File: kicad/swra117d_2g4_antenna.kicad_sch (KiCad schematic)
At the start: 5 parts, among them J1 SMA edge launch

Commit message: Fix the ERC error and the lib_symbol_mismatch warnings
A KiCad 9 ERC run reported 1 error and 8 warnings, all from where the
schematic's symbols come from rather than from its wiring.

power_pin_not_driven on #PWR01: the board is entirely passive, so nothing
drives the ground net as far as ERC is concerned. Added #FLG01, a PWR_FLAG
with a power-output pin, on that net.

lib_symbol_mismatch on C1, C2, L1, J1 and the four ground symbols: a
schematic embeds a copy of every symbol it places, and the embedded
stand-ins for Device:C, Device:L, Connector:Conn_Coaxial and power:GND did
not match the installed stock libraries. Moved all of them into
library/SWRA117D_RF.kicad_sym with the same pin geometry, so the schematic
embeds from an in-repo library and the two copies are identical by
construction - the same reason the antenna symbol never produced the
warning. The project no longer depends on the stock libraries at all.

check_project.py now enforces exactly that condition: every embedded symbol
must resolve to the project library and compare equal to it, and any
external lib_id is an error. Both cases are covered by mutation tests.

Nothing in the ERC report touched connectivity - the netlist was as
designed. DRC has not been run yet.

Co-Authored-By: Claude Opus 5 <noreply@anthropic.com>
Claude-Session: https://claude.ai/code/session_01Prj6bUQ2KQzzxzD4bgtswJ
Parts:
- C1, C2: symbol Device:C -> SWRA117D_RF:C
- J1: symbol Connector:Conn_Coaxial -> SWRA117D_RF:Conn_Coaxial_SMA
- L1: symbol Device:L -> SWRA117D_RF:L
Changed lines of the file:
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@@
+		(stroke (width 0) (type default))
+	)
+	(wire
+		(pts (xy 91.44 102.87) (xy 86.36 102.87))
 		(stroke (width 0) (type default))
 	)
@@
 	)
 	(symbol
-		(lib_id "Connector:Conn_Coaxial")
+		(lib_id "SWRA117D_RF:Conn_Coaxial_SMA")
 		(at 76.2 88.9 0)
 		(unit 1)
@@
 	)
 	(symbol
-		(lib_id "Device:C")
+		(lib_id "SWRA117D_RF:C")
 		(at 91.44 96.52 0)
 		(unit 1)
@@
 	)
 	(symbol
-		(lib_id "Device:L")
+		(lib_id "SWRA117D_RF:L")
 		(at 101.6 88.9 90)
 		(unit 1)
@@
 	)
 	(symbol
-		(lib_id "Device:C")
+		(lib_id "SWRA117D_RF:C")
 		(at 111.76 96.52 0)
 		(unit 1)
@@
 	)
 	(symbol
-		(lib_id "power:GND")
+		(lib_id "SWRA117D_RF:GND")
 		(at 76.2 96.52 0)
 		(unit 1)
@@
 	)
 	(symbol
-		(lib_id "power:GND")
+		(lib_id "SWRA117D_RF:GND")
 		(at 91.44 102.87 0)
 		(unit 1)
@@
 	)
 	(symbol
-		(lib_id "power:GND")
+		(lib_id "SWRA117D_RF:GND")
 		(at 111.76 102.87 0)
 		(unit 1)
@@
 	)
 	(symbol
-		(lib_id "power:GND")
+		(lib_id "SWRA117D_RF:GND")
 		(at 129.54 96.52 0)
 		(unit 1)
@@
 			)
 		)
+	)
+	(symbol
+		(lib_id "SWRA117D_RF:PWR_FLAG")
+		(at 86.36 102.87 0)
+		(unit 1)
+		(exclude_from_sim yes)
+		(in_bom no)
+		(on_board no)
+		(dnp no)
+		(property "Reference" "#FLG01"
+			(at 86.36 109.22 0)
+			(effects (font (size 1.27 1.27)) (hide yes))
+		)
+		(property "Value" "PWR_FLAG" (at 86.36 99.06 0) (effects (font (size 1.27 1.27))))
+		(property "Footprint" "" (at 86.36 102.87 0) (effects (font (size 1.27 1.27)) (hide yes)))
+		(property "Datasheet" "" (at 86.36 102.87 0) (effects (font (size 1.27 1.27)) (hide yes)))
+		(property "Description" "ERC power source flag"
+			(at 86.36 102.87 0)
+			(effects (font (size 1.27 1.27)) (hide yes))
+		)
+		(pin "1")
+		(instances
+			(project "swra117d_2g4_antenna"
+				(path "/0c52b35a-5623-5f55-988d-762afc65fb88" (reference "#FLG01") (unit 1))
+			)
+		)

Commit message: Ship the board unmatched: L1 is a 0 ohm jumper
The SWRA117D antenna is a 50 ohm design, so the board should leave the
factory with nothing matched out. L1 was defaulting to the 0.8 nH the
lumped model prefers, which put reactance in the path of an antenna that
does not need it. L1 is now a 0 ohm jumper and C1/C2 stay unpopulated, so
the RF path is connector -> 50 ohm line -> antenna and the pi network is
three empty footprints kept for retuning the assembled product.

The ngspice testbench now defaults to the as-built population (l1=1p) and
documents the 0.8 nH case as a comparison. Unmatched, the model clears
-10 dB over the whole ISM band (-10.5 dB at 2.400 GHz, -26.3 dB at
2.4835 GHz, best -29 dB at 2.493 GHz), which is the evidence that no match
is needed; 0.8 nH buys ~8 dB at band centre and moves resonance 30 MHz
down. README documents both columns and why the footprints exist at all:
stackup, ground plane size, FR4 tolerance and enclosure loading.

No change to nets, pads or routing.

Co-Authored-By: Claude Opus 5 <noreply@anthropic.com>
Claude-Session: https://claude.ai/code/session_01Prj6bUQ2KQzzxzD4bgtswJ
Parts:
- L1: value 0.8nH -> 0R
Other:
- note added: "RF test board for the TI SWRA117D 2.45 GHz printed inverted-F antenna. J1 feeds a 1.5 mm wide 50 ohm microstrip on 0.8 mm FR4 (er 4.4, tan d 0.02). The antenna is a 50 ohm design, so the board ships unmatched: L1 is a 0 ohm jumper and C1 / C2 are unpopulated. The pi network is there to retune the antenna once it is measured in its real enclosure - fit parts only then. AE1 pin 2 must sit on the gr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"
- note removed: "RF test board for the TI SWRA117D 2.45 GHz printed inverted-F antenna. J1 feeds a 1.5 mm wide 50 ohm microstrip on 0.8 mm FR4 (er 4.4, tan d 0.02). C1 / L1 / C2 form a pi matching network; only L1 is fitted by default. AE1 pin 2 must sit on the ground plane edge - see the keep-out on the PCB. Simulation: sim/s11_pi_match.cir (ngspice, lumped antenna model) and sim/openems/swra117d_openems.py (ful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"
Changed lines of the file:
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@@
 		(effects (font (size 1.27 1.27)) (justify left bottom))
 	)
-	(text "RF test board for the TI SWRA117D 2.45 GHz printed inverted-F antenna.\n\nJ1 feeds a 1.5 mm wide 50 ohm microstrip on 0.8 mm FR4 (er 4.4, tan d 0.02).\nC1 / L1 / C2 form a pi matching network; only L1 is fitted by default.\nAE1 pin 2 must sit on the ground plane edge - see the keep-out on the PCB.\n\nSimulation: sim/s11_pi_match.cir (ngspice, lumped antenna model) and\nsim/openems/swra117d_openems.py (full wave S11, impedance, far field)."
+	(text "RF test board for the TI SWRA117D 2.45 GHz printed inverted-F antenna.\n\nJ1 feeds a 1.5 mm wide 50 ohm microstrip on 0.8 mm FR4 (er 4.4, tan d 0.02).\nThe antenna is a 50 ohm design, so the board ships unmatched: L1 is a 0 ohm\njumper and C1 / C2 are unpopulated. The pi network is there to retune the\nantenna once it is measured in its real enclosure - fit parts only then.\nAE1 pin 2 must sit on the ground plane edge - see the keep-out on the PCB.\n\nSimulation: sim/s11_pi_match.cir (ngspice, lumped antenna model) and\nsim/openems/swra117d_openems.py (full wave S11, impedance, far field)."
 		(exclude_from_sim no)
 		(at 76.2 112 0)
@@
 			(effects (font (size 1.27 1.27)) (justify left))
 		)
-		(property "Value" "0.8nH" (at 101.6 92.71 0) (effects (font (size 1.27 1.27)) (justify left)))
+		(property "Value" "0R" (at 101.6 92.71 0) (effects (font (size 1.27 1.27)) (justify left)))
 		(property "Footprint" "SWRA117D_RF:Chip_0402_1005Metric_RF"
 			(at 101.6 88.9 0)
@@
 		)
 		(property "Datasheet" "~" (at 101.6 88.9 0) (effects (font (size 1.27 1.27)) (hide yes)))
-		(property "Description" "Series element of the pi matching network"
+		(property "Description" "Series element of the pi matching network; 0 ohm jumper as built"
 			(at 101.6 88.9 0)
 			(effects (font (size 1.27 1.27)) (hide yes))

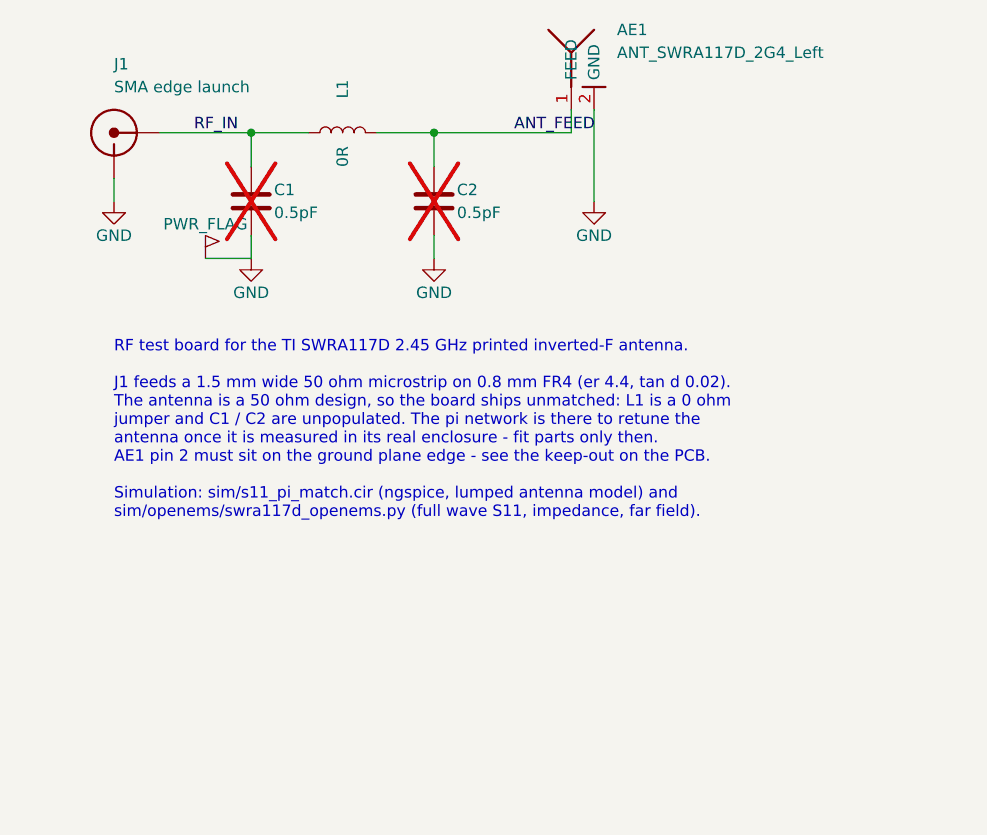
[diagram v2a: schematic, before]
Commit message: Feed the radiator straight from the SMA port, drop the matching network
The SWRA117D antenna is a 50 ohm design, so the board now goes connector ->
50 ohm line -> radiator with nothing in between. C1, L1 and C2 are gone
from the schematic and the board, RF_IN and ANT_FEED collapse into one net
ANT_FEED, and the feed is a single 1.5 mm microstrip run of 32.1 mm from
the SMA signal pad to the antenna feed pad: one 45 degree corner and a
1 mm neck down to 0.5 mm to meet the feed pad. A 0 ohm jumper would still
have added a few tenths of a nH and two pad discontinuities, which is the
wrong thing to have in the path when the point is to measure the antenna.

The 0402 land and the C/L symbols stay in the libraries, and the pi
topology stays in the ngspice deck as a comment, so a match can be worked
out and added if the enclosed product needs one.

Simulation now mirrors the board:
- sim/s11_pi_match.cir -> sim/s11_antenna.cir: antenna behind a lossless
  50 ohm T line (32.1 mm, TD = 195 ps), so S11 is referenced to the
  connector like a VNA measurement. -10.5 dB at 2.400 GHz, -15.4 dB at
  2.442 GHz, -26.4 dB at 2.4835 GHz, best -28.8 dB at 2.493 GHz, under
  -10 dB from 2.394 to 2.595 GHz. The line rotates Zin 172 degrees but
  cannot change |S11|, which is why the lumped model still answers the
  return-loss question.
- openEMS: the model no longer assumes a straight feed. It reads the actual
  track segments and their widths, launches the port at the board edge in
  place of the connector, and rebuilds the top pour as boxes around the
  keep-away corridors it reads from the rule areas (6 boxes, 2 corridors).

Also: the schematic now embeds only the symbols it places (4, was 6),
which is what KiCad writes itself.

Co-Authored-By: Claude Opus 5 <noreply@anthropic.com>
Claude-Session: https://claude.ai/code/session_01Prj6bUQ2KQzzxzD4bgtswJ
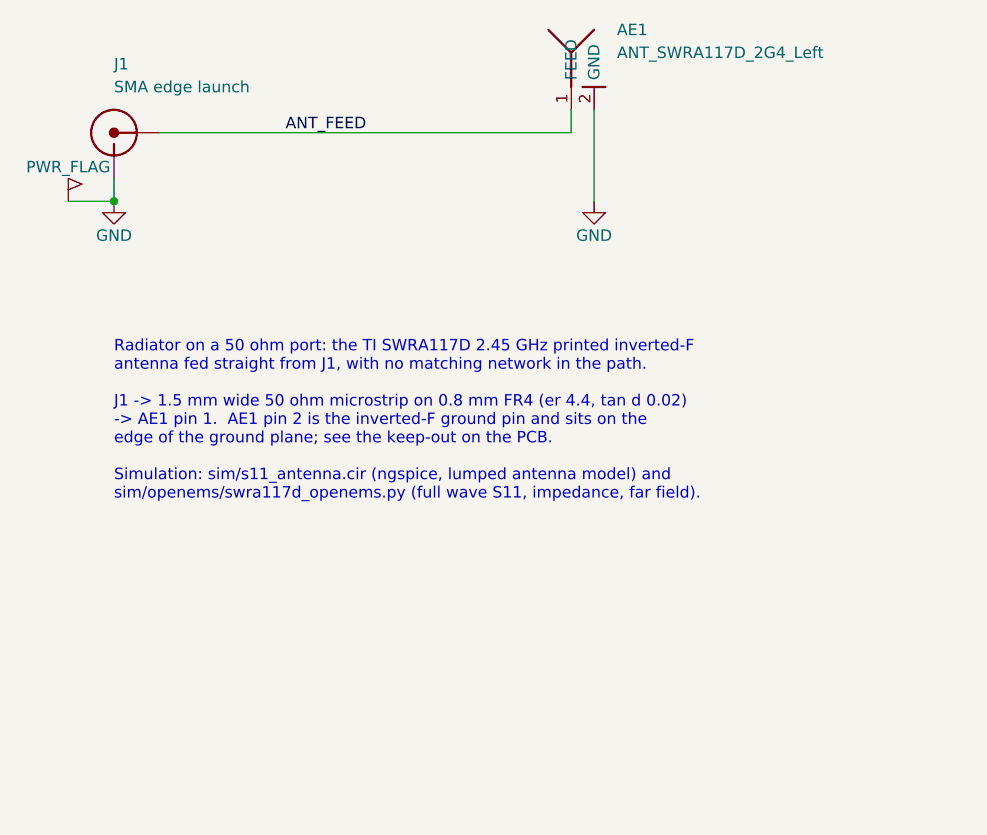
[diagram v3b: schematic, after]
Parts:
- removed C1, C2: 0.5pF, SWRA117D_RF:Chip_0402_1005Metric_RF, symbol SWRA117D_RF:C
- removed L1: 0R, SWRA117D_RF:Chip_0402_1005Metric_RF, symbol SWRA117D_RF:L
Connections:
- net RF_IN is gone; now on net ANT_FEED: J1.1 (In)
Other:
- note added: "Radiator on a 50 ohm port: the TI SWRA117D 2.45 GHz printed inverted-F antenna fed straight from J1, with no matching network in the path. J1 -> 1.5 mm wide 50 ohm microstrip on 0.8 mm FR4 (er 4.4, tan d 0.02) -> AE1 pin 1. AE1 pin 2 is the inverted-F ground pin and sits on the edge of the ground plane; see the keep-out on the PCB. Simulation: sim/s11_antenna.cir (ngspice, lumped antenna model) a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"
- note removed: "RF test board for the TI SWRA117D 2.45 GHz printed inverted-F antenna. J1 feeds a 1.5 mm wide 50 ohm microstrip on 0.8 mm FR4 (er 4.4, tan d 0.02). The antenna is a 50 ohm design, so the board ships unmatched: L1 is a 0 ohm jumper and C1 / C2 are unpopulated. The pi network is there to retune the antenna once it is measured in its real enclosure - fit parts only then. AE1 pin 2 must sit on the gr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"
- title: 2.45 GHz PCB antenna (TI SWRA117D) - RF test board -> 2.45 GHz PCB antenna (TI SWRA117D) - radiator on a 50 ohm SMA port
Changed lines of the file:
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@@
 	(paper "A4")
 	(title_block
-		(title "2.45 GHz PCB antenna (TI SWRA117D) - RF test board")
+		(title "2.45 GHz PCB antenna (TI SWRA117D) - radiator on a 50 ohm SMA port")
 		(date "2026-09-12")
 		(rev "A")
-		(comment 1 "50 ohm microstrip feed + pi matching network")
+		(comment 1 "Radiator fed straight from the SMA port, no matching network")
 		(comment 2 "Antenna keep-out: no copper on any layer")
 	)
 	(wire
-		(pts (xy 81.28 88.9) (xy 91.44 88.9))
-		(stroke (width 0) (type default))
-	)
-	(wire
-		(pts (xy 91.44 88.9) (xy 97.79 88.9))
-		(stroke (width 0) (type default))
-	)
-	(wire
-		(pts (xy 105.41 88.9) (xy 111.76 88.9))
-		(stroke (width 0) (type default))
-	)
-	(wire
-		(pts (xy 111.76 88.9) (xy 127 88.9))
+		(pts (xy 81.28 88.9) (xy 127 88.9))
 		(stroke (width 0) (type default))
 	)
@@
 	)
 	(wire
-		(pts (xy 91.44 88.9) (xy 91.44 92.71))
+		(pts (xy 76.2 93.98) (xy 76.2 96.52))
 		(stroke (width 0) (type default))
 	)
 	(wire
-		(pts (xy 91.44 100.33) (xy 91.44 102.87))
-		(stroke (width 0) (type default))
-	)
-	(wire
-		(pts (xy 111.76 88.9) (xy 111.76 92.71))
-		(stroke (width 0) (type default))
-	)
-	(wire
-		(pts (xy 111.76 100.33) (xy 111.76 102.87))
-		(stroke (width 0) (type default))
-	)
-	(wire
-		(pts (xy 76.2 93.98) (xy 76.2 96.52))
+		(pts (xy 76.2 96.52) (xy 71.12 96.52))
 		(stroke (width 0) (type default))
 	)
@@
 		(stroke (width 0) (type default))
 	)
-	(wire
-		(pts (xy 91.44 102.87) (xy 86.36 102.87))
-		(stroke (width 0) (type default))
-	)
 	(junction
-		(at 91.44 88.9)
+		(at 76.2 96.52)
 		(diameter 0)
 		(color 0 0 0 0)
 	)
-	(junction
-		(at 111.76 88.9)
-		(diameter 0)
-		(color 0 0 0 0)
-	)
-	(label "RF_IN"
-		(at 85.09 88.9 0)
+	(label "ANT_FEED"
+		(at 95.25 88.9 0)
 		(effects (font (size 1.27 1.27)) (justify left bottom))
 	)
-	(label "ANT_FEED"
-		(at 120.65 88.9 0)
-		(effects (font (size 1.27 1.27)) (justify left bottom))
-	)
-	(text "RF test board for the TI SWRA117D 2.45 GHz printed inverted-F antenna.\n\nJ1 feeds a 1.5 mm wide 50 ohm microstrip on 0.8 mm FR4 (er 4.4, tan d 0.02).\nThe antenna is a 50 ohm design, so the board ships unmatched: L1 is a 0 ohm\njumper and C1 / C2 are unpopulated. The pi network is there to retune the\nantenna once it is measured in its real enclosure - fit parts only then.\nAE1 pin 2 must sit on the ground plane edge - see the keep-out on the PCB.\n\nSimulation: sim/s11_pi_match.cir (ngspice, lumped antenna model) and\nsim/openems/swra117d_openems.py (full wave S11, impedance, far field)."
+	(text "Radiator on a 50 ohm port: the TI SWRA117D 2.45 GHz printed inverted-F\nantenna fed straight from J1, with no matching network in the path.\n\nJ1 -> 1.5 mm wide 50 ohm microstrip on 0.8 mm FR4 (er 4.4, tan d 0.02)\n-> AE1 pin 1.  AE1 pin 2 is the inverted-F ground pin and sits on the\nedge of the ground plane; see the keep-out on the PCB.\n\nSimulation: sim/s11_antenna.cir (ngspice, lumped antenna model) and\nsim/openems/swra117d_openems.py (full wave S11, impedance, far field)."
 		(exclude_from_sim no)
 		(at 76.2 112 0)
@@
 			(project "swra117d_2g4_antenna"
 				(path "/0c52b35a-5623-5f55-988d-762afc65fb88" (reference "J1") (unit 1))
-			)
-		)
-	)
-	(symbol
-		(lib_id "SWRA117D_RF:C")
-		(at 91.44 96.52 0)
-		(unit 1)
-		(exclude_from_sim no)
-		(in_bom yes)
-		(on_board yes)
-		(dnp yes)
-		(property "Reference" "C1"
-			(at 93.98 95.25 0)
-			(effects (font (size 1.27 1.27)) (justify left))
-		)
-		(property "Value" "0.5pF" (at 93.98 97.79 0) (effects (font (size 1.27 1.27)) (justify left)))
-		(property "Footprint" "SWRA117D_RF:Chip_0402_1005Metric_RF"
-			(at 91.44 96.52 0)
-			(effects (font (size 1.27 1.27)) (hide yes))
-		)
-		(property "Datasheet" "~" (at 91.44 96.52 0) (effects (font (size 1.27 1.27)) (hide yes)))
-		(property "Description" "Shunt element of the pi matching network (source side)"
-			(at 91.44 96.52 0)
-			(effects (font (size 1.27 1.27)) (hide yes))
-		)
-		(pin "1")
-		(pin "2")
-		(instances
-			(project "swra117d_2g4_antenna"
-				(path "/0c52b35a-5623-5f55-988d-762afc65fb88" (reference "C1") (unit 1))
-			)
-		)
-	)
-	(symbol
-		(lib_id "SWRA117D_RF:L")
-		(at 101.6 88.9 90)
-		(unit 1)
-		(exclude_from_sim no)
-		(in_bom yes)
-		(on_board yes)
-		(dnp no)
-		(property "Reference" "L1"
-			(at 101.6 85.09 0)
-			(effects (font (size 1.27 1.27)) (justify left))
-		)
-		(property "Value" "0R" (at 101.6 92.71 0) (effects (font (size 1.27 1.27)) (justify left)))
-		(property "Footprint" "SWRA117D_RF:Chip_0402_1005Metric_RF"
-			(at 101.6 88.9 0)
-			(effects (font (size 1.27 1.27)) (hide yes))
-		)
-		(property "Datasheet" "~" (at 101.6 88.9 0) (effects (font (size 1.27 1.27)) (hide yes)))
-		(property "Description" "Series element of the pi matching network; 0 ohm jumper as built"
-			(at 101.6 88.9 0)
-			(effects (font (size 1.27 1.27)) (hide yes))
-		)
-		(pin "1")
-		(pin "2")
-		(instances
-			(project "swra117d_2g4_antenna"
-				(path "/0c52b35a-5623-5f55-988d-762afc65fb88" (reference "L1") (unit 1))
-			)
-		)
-	)
-	(symbol
-		(lib_id "SWRA117D_RF:C")
-		(at 111.76 96.52 0)
-		(unit 1)
-		(exclude_from_sim no)
-		(in_bom yes)
-		(on_board yes)
-		(dnp yes)
-		(property "Reference" "C2"
-			(at 114.3 95.25 0)
-			(effects (font (size 1.27 1.27)) (justify left))
-		)
-		(property "Value" "0.5pF" (at 114.3 97.79 0) (effects (font (size 1.27 1.27)) (justify left)))
-		(property "Footprint" "SWRA117D_RF:Chip_0402_1005Metric_RF"
-			(at 111.76 96.52 0)
-			(effects (font (size 1.27 1.27)) (hide yes))
-		)
-		(property "Datasheet" "~" (at 111.76 96.52 0) (effects (font (size 1.27 1.27)) (hide yes)))
-		(property "Description" "Shunt element of the pi matching network (antenna side)"
-			(at 111.76 96.52 0)
-			(effects (font (size 1.27 1.27)) (hide yes))
-		)
-		(pin "1")
-		(pin "2")
-		(instances
-			(project "swra117d_2g4_antenna"
-				(path "/0c52b35a-5623-5f55-988d-762afc65fb88" (reference "C2") (unit 1))
 			)
 		)
@@
 	(symbol
 		(lib_id "SWRA117D_RF:GND")
-		(at 91.44 102.87 0)
+		(at 129.54 96.52 0)
 		(unit 1)
 		(exclude_from_sim no)
@@
 		(dnp no)
 		(property "Reference" "#PWR02"
-			(at 91.44 109.22 0)
-			(effects (font (size 1.27 1.27)) (hide yes))
-		)
-		(property "Value" "GND" (at 91.44 106.68 0) (effects (font (size 1.27 1.27))))
-		(property "Footprint" "" (at 91.44 102.87 0) (effects (font (size 1.27 1.27)) (hide yes)))
-		(property "Datasheet" "" (at 91.44 102.87 0) (effects (font (size 1.27 1.27)) (hide yes)))
-		(property "Description" "Ground reference"
-			(at 91.44 102.87 0)
-			(effects (font (size 1.27 1.27)) (hide yes))
-		)
-		(pin "1")
-		(instances
-			(project "swra117d_2g4_antenna"
-				(path "/0c52b35a-5623-5f55-988d-762afc65fb88" (reference "#PWR02") (unit 1))
-			)
-		)
-	)
-	(symbol
-		(lib_id "SWRA117D_RF:GND")
-		(at 111.76 102.87 0)
-		(unit 1)
-		(exclude_from_sim no)
-		(in_bom yes)
-		(on_board yes)
-		(dnp no)
-		(property "Reference" "#PWR03"
-			(at 111.76 109.22 0)
-			(effects (font (size 1.27 1.27)) (hide yes))
-		)
-		(property "Value" "GND" (at 111.76 106.68 0) (effects (font (size 1.27 1.27))))
-		(property "Footprint" "" (at 111.76 102.87 0) (effects (font (size 1.27 1.27)) (hide yes)))
-		(property "Datasheet" "" (at 111.76 102.87 0) (effects (font (size 1.27 1.27)) (hide yes)))
-		(property "Description" "Ground reference"
-			(at 111.76 102.87 0)
-			(effects (font (size 1.27 1.27)) (hide yes))
-		)
-		(pin "1")
-		(instances
-			(project "swra117d_2g4_antenna"
-				(path "/0c52b35a-5623-5f55-988d-762afc65fb88" (reference "#PWR03") (unit 1))
-			)
-		)
-	)
-	(symbol
-		(lib_id "SWRA117D_RF:GND")
-		(at 129.54 96.52 0)
-		(unit 1)
-		(exclude_from_sim no)
-		(in_bom yes)
-		(on_board yes)
-		(dnp no)
-		(property "Reference" "#PWR04"
 			(at 129.54 102.87 0)
 			(effects (font (size 1.27 1.27)) (hide yes))
@@
 		(instances
 			(project "swra117d_2g4_antenna"
-				(path "/0c52b35a-5623-5f55-988d-762afc65fb88" (reference "#PWR04") (unit 1))
+				(path "/0c52b35a-5623-5f55-988d-762afc65fb88" (reference "#PWR02") (unit 1))
 			)
 		)
@@
 	(symbol
 		(lib_id "SWRA117D_RF:PWR_FLAG")
-		(at 86.36 102.87 0)
+		(at 71.12 96.52 0)
 		(unit 1)
 		(exclude_from_sim yes)
@@
 		(dnp no)
 		(property "Reference" "#FLG01"
-			(at 86.36 109.22 0)
+			(at 71.12 102.87 0)
 			(effects (font (size 1.27 1.27)) (hide yes))
 		)
-		(property "Value" "PWR_FLAG" (at 86.36 99.06 0) (effects (font (size 1.27 1.27))))
-		(property "Footprint" "" (at 86.36 102.87 0) (effects (font (size 1.27 1.27)) (hide yes)))
-		(property "Datasheet" "" (at 86.36 102.87 0) (effects (font (size 1.27 1.27)) (hide yes)))
+		(property "Value" "PWR_FLAG" (at 71.12 92.71 0) (effects (font (size 1.27 1.27))))
+		(property "Footprint" "" (at 71.12 96.52 0) (effects (font (size 1.27 1.27)) (hide yes)))
+		(property "Datasheet" "" (at 71.12 96.52 0) (effects (font (size 1.27 1.27)) (hide yes)))
 		(property "Description" "ERC power source flag"
-			(at 86.36 102.87 0)
+			(at 71.12 96.52 0)
 			(effects (font (size 1.27 1.27)) (hide yes))
 		)
